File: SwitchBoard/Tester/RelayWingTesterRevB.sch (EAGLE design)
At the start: 22 parts

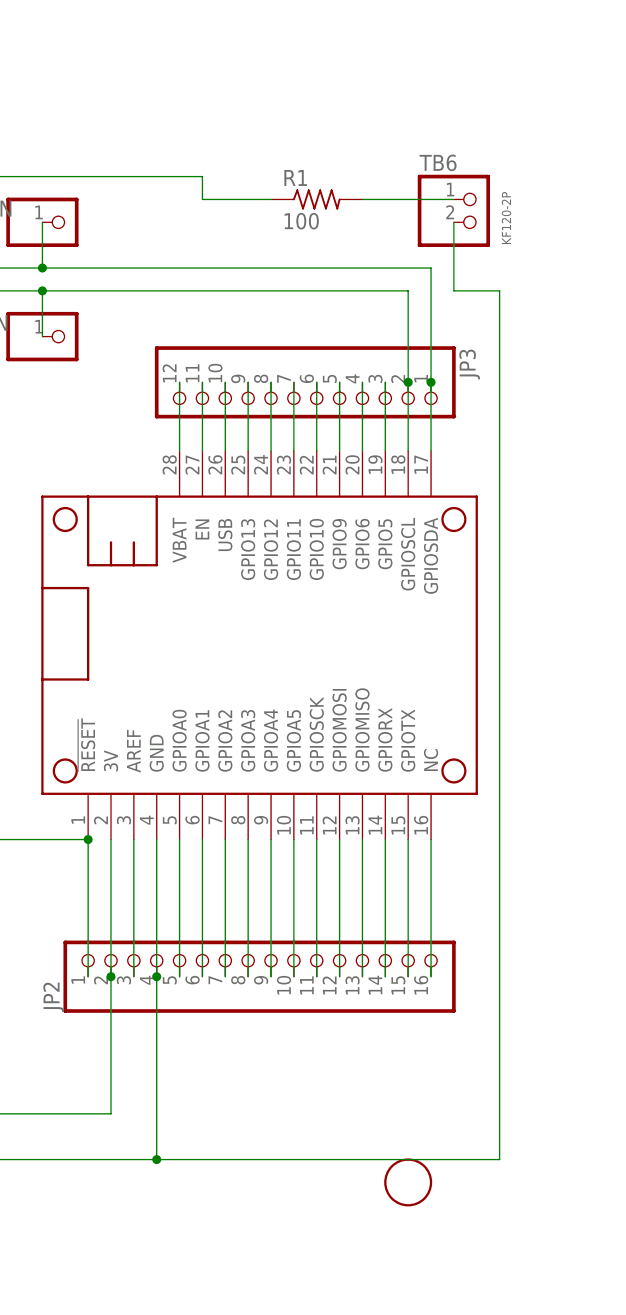
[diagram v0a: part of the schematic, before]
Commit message: Moved resistor to the ground-side of the current sensor
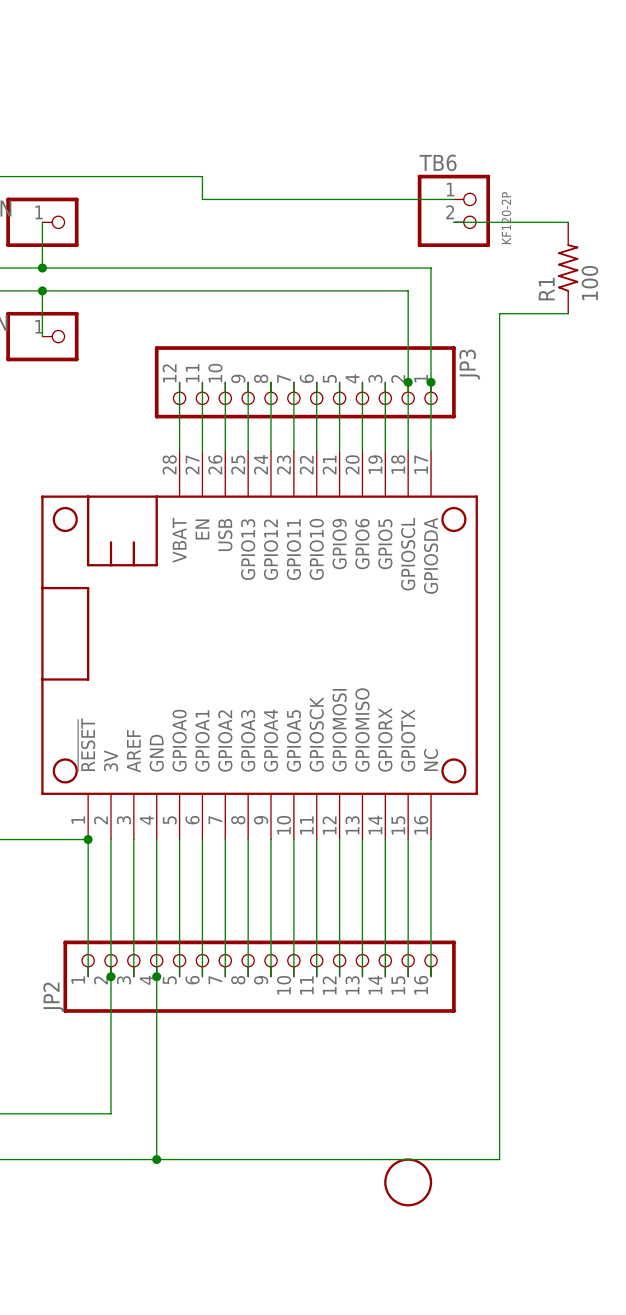
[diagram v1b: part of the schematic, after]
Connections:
- removed net N$54: R1.2, TB6.1
- new net N$18: R1.2, TB6.2
- net GND: now also R1.1; no longer TB6.2
- net N$53: now also TB6.1; no longer R1.1
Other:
- moved on the sheet: R1
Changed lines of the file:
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@@
 </instance>
 <instance part="U$4" gate="G$1" x="81.28" y="111.76" smashed="yes"/>
-<instance part="R1" gate="G$1" x="223.52" y="144.78" smashed="yes">
-<attribute name="NAME" x="219.71" y="146.2786" size="1.778" layer="95"/>
-<attribute name="VALUE" x="219.71" y="141.478" size="1.778" layer="96"/>
+<instance part="R1" gate="G$1" x="251.46" y="137.16" smashed="yes" rot="R90">
+<attribute name="NAME" x="249.9614" y="133.35" size="1.778" layer="95" rot="R90"/>
+<attribute name="VALUE" x="254.762" y="133.35" size="1.778" layer="96" rot="R90"/>
 </instance>
 <instance part="LED1" gate="G$1" x="88.9" y="154.94" smashed="yes" rot="R90">
@@
 <wire x1="205.74" y1="38.1" x2="205.74" y2="58.42" width="0.1524" layer="91"/>
 <junction x="205.74" y="58.42"/>
-<pinref part="TB6" gate="G$1" pin="2"/>
-<wire x1="238.76" y1="142.24" x2="238.76" y2="134.62" width="0.1524" layer="91"/>
-<wire x1="238.76" y1="134.62" x2="243.84" y2="134.62" width="0.1524" layer="91"/>
-<wire x1="243.84" y1="134.62" x2="243.84" y2="38.1" width="0.1524" layer="91"/>
+<wire x1="243.84" y1="132.08" x2="243.84" y2="38.1" width="0.1524" layer="91"/>
 <wire x1="243.84" y1="38.1" x2="205.74" y2="38.1" width="0.1524" layer="91"/>
 <junction x="205.74" y="38.1"/>
@@
 <wire x1="177.8" y1="43.18" x2="177.8" y2="38.1" width="0.1524" layer="91"/>
 <junction x="177.8" y="38.1"/>
+<pinref part="R1" gate="G$1" pin="1"/>
+<wire x1="251.46" y1="132.08" x2="243.84" y2="132.08" width="0.1524" layer="91"/>
 </segment>
 </net>
@@
 <wire x1="109.22" y1="147.32" x2="210.82" y2="147.32" width="0.1524" layer="91"/>
 <wire x1="210.82" y1="147.32" x2="210.82" y2="144.78" width="0.1524" layer="91"/>
-<pinref part="R1" gate="G$1" pin="1"/>
-<wire x1="210.82" y1="144.78" x2="218.44" y2="144.78" width="0.1524" layer="91"/>
-</segment>
-</net>
-<net name="N$54" class="0">
-<segment>
-<pinref part="R1" gate="G$1" pin="2"/>
 <pinref part="TB6" gate="G$1" pin="1"/>
-<wire x1="228.6" y1="144.78" x2="238.76" y2="144.78" width="0.1524" layer="91"/>
+<wire x1="210.82" y1="144.78" x2="238.76" y2="144.78" width="0.1524" layer="91"/>
 </segment>
 </net>
@@
 </segment>
 </net>
+<net name="N$18" class="0">
+<segment>
+<pinref part="TB6" gate="G$1" pin="2"/>
+<pinref part="R1" gate="G$1" pin="2"/>
+<wire x1="238.76" y1="142.24" x2="251.46" y2="142.24" width="0.1524" layer="91"/>
+</segment>
+</net>
